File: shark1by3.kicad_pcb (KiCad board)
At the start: 2 copper layers, 57.2 x 46 mm, 26 parts, among them SW1 SW_Push_Reset, U1 PRTR5V0U2X, U2 ATmega32U4-A, X1 16MHz

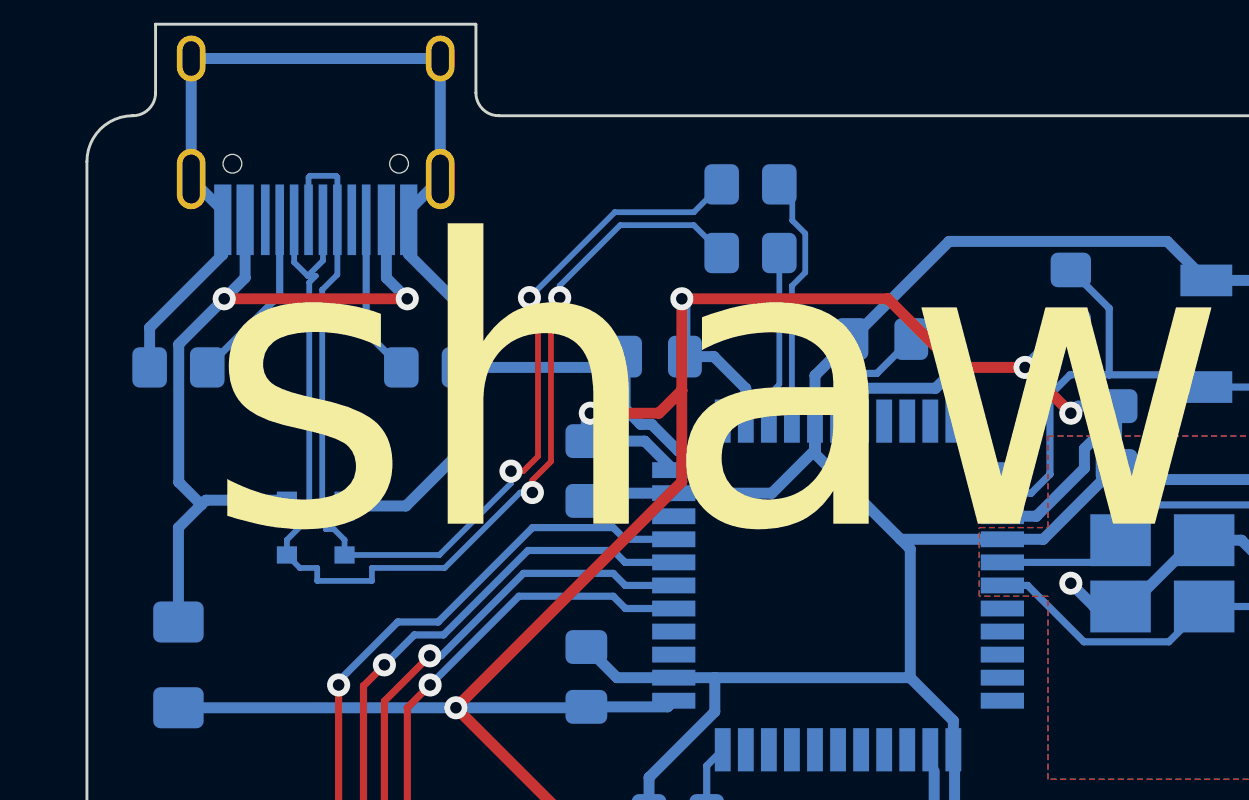
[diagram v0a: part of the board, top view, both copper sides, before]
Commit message: shorten data lines
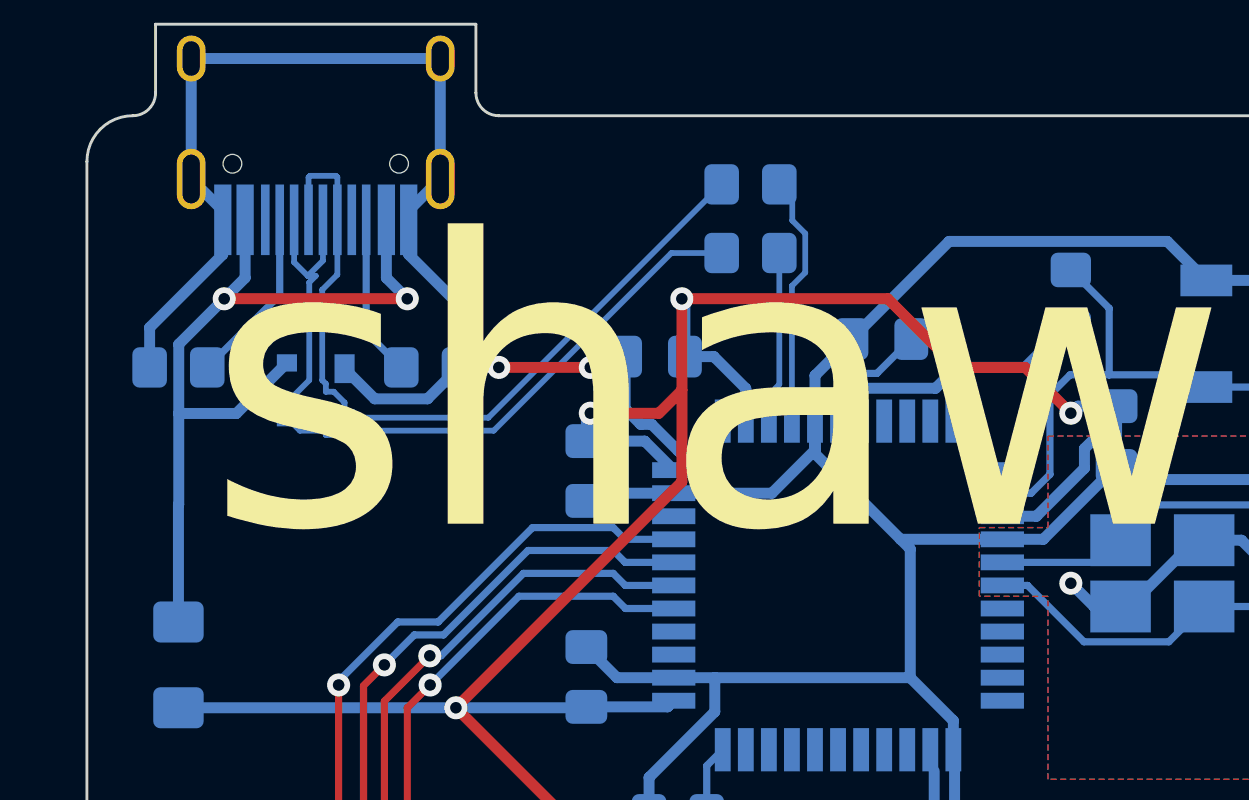
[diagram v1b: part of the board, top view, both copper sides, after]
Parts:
- moved U1 4.76 mm to (134.9, 120.7)
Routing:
- net DN: track 39.8 -> 28.0 mm, vias 2 -> 0
- net DP: track 38.6 -> 28.0 mm, vias 2 -> 0
- net GND: track 157.0 -> 154.2 mm, vias 3 -> 5
- net +5V: track 101.2 -> 103.6 mm, vias 7 -> 6
- net VCC: track 28.0 -> 28.8 mm

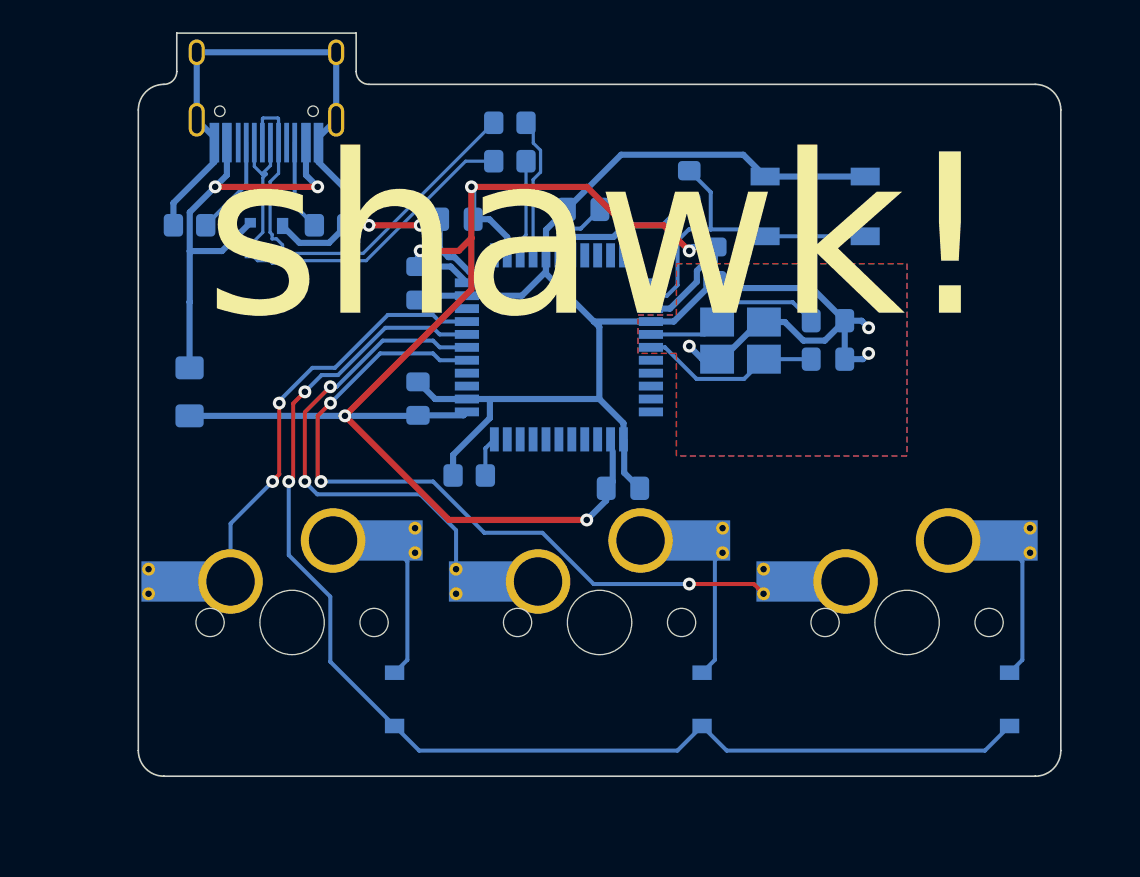
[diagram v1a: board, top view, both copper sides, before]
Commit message: add scuffed mounting holes
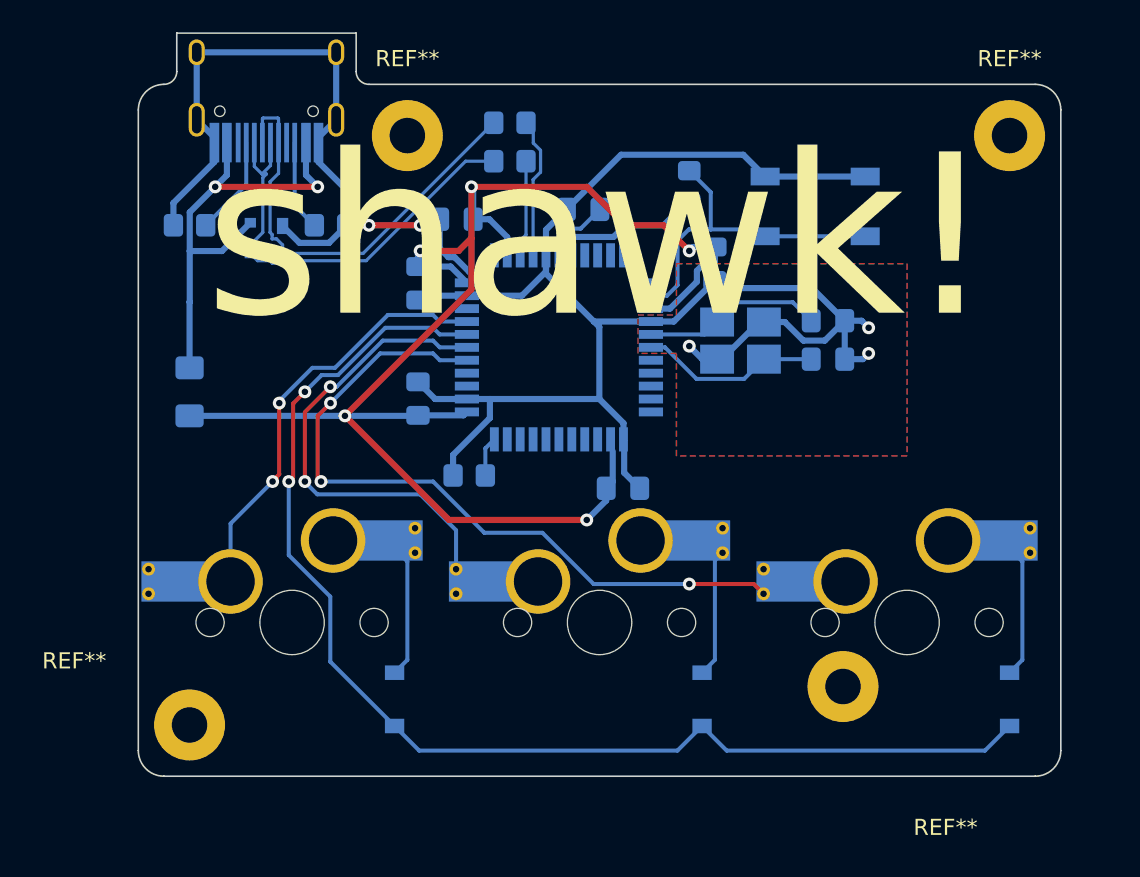
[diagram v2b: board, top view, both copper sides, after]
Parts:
- added REF**: MountingHole_2.2mm_M2_Pad, MountingHole:MountingHole_2.2mm_M2_Pad, F.Cu at (181.0, 114.3)
- added REF**: MountingHole_2.2mm_M2_Pad, MountingHole:MountingHole_2.2mm_M2_Pad, F.Cu at (170.7, 148.4)
- added REF**: MountingHole_2.2mm_M2_Pad, MountingHole:MountingHole_2.2mm_M2_Pad, F.Cu at (130.2, 150.8)
- added REF**: MountingHole_2.2mm_M2_Pad, MountingHole:MountingHole_2.2mm_M2_Pad, F.Cu at (143.7, 114.3)
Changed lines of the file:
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@@
   (net 44 "DN")
   (net 45 "DP")
+  (footprint "MountingHole:MountingHole_2.2mm_M2_Pad" (layer "F.Cu")
+    (at 180.975 114.3)
+    (descr "Mounting Hole 2.2mm, M2")
+    (tags "mounting hole 2.2mm m2")
+    (attr exclude_from_pos_files exclude_from_bom)
+    (fp_text reference "REF**" (at 0 -4.7625) (layer "F.SilkS")
+      (effects (font (size 1 1) (thickness 0.15)))
+    )
+    (fp_text value "MountingHole_2.2mm_M2_Pad" (at 0 3.2) (layer "F.Fab")
+      (effects (font (size 1 1) (thickness 0.15)))
+    )
+    (fp_text user "${REFERENCE}" (at 0 0) (layer "F.Fab")
+      (effects (font (size 1 1) (thickness 0.15)))
+    )
+    (fp_circle (center 0 0) (end 2.2 0) (layer "Cmts.User") (width 0.15) (fill none))
+    (fp_circle (center 0 0) (end 2.45 0) (layer "F.CrtYd") (width 0.05) (fill none))
+    (pad "1" thru_hole circle (at 0 0) (size 4.4 4.4) (drill 2.2) (layers *.Cu *.Mask))
+  )
   (footprint "MX_Only:MXOnly-1U-Hotswap-Antishear" (layer "F.Cu")
     (at 174.625 144.4625)
@@
     )
   )
+  (footprint "MountingHole:MountingHole_2.2mm_M2_Pad" (layer "F.Cu")
+    (at 170.65625 148.43125)
+    (descr "Mounting Hole 2.2mm, M2")
+    (tags "mounting hole 2.2mm m2")
+    (attr exclude_from_pos_files exclude_from_bom)
+    (fp_text reference "REF**" (at 6.35 8.73125) (layer "F.SilkS")
+      (effects (font (size 1 1) (thickness 0.15)))
+    )
+    (fp_text value "MountingHole_2.2mm_M2_Pad" (at 0 3.2) (layer "F.Fab")
+      (effects (font (size 1 1) (thickness 0.15)))
+    )
+    (fp_text user "${REFERENCE}" (at 0 0) (layer "F.Fab")
+      (effects (font (size 1 1) (thickness 0.15)))
+    )
+    (fp_circle (center 0 0) (end 2.2 0) (layer "Cmts.User") (width 0.15) (fill none))
+    (fp_circle (center 0 0) (end 2.45 0) (layer "F.CrtYd") (width 0.05) (fill none))
+    (pad "1" thru_hole circle (at 0 0) (size 4.4 4.4) (drill 2.2) (layers *.Cu *.Mask))
+  )
   (footprint "MX_Only:MXOnly-1U-Hotswap-Antishear" (layer "F.Cu")
     (at 155.575 144.4625)
@@
     )
   )
+  (footprint "MountingHole:MountingHole_2.2mm_M2_Pad" (layer "F.Cu")
+    (at 130.175 150.8125)
+    (descr "Mounting Hole 2.2mm, M2")
+    (tags "mounting hole 2.2mm m2")
+    (attr exclude_from_pos_files exclude_from_bom)
+    (fp_text reference "REF**" (at -7.14375 -3.96875) (layer "F.SilkS")
+      (effects (font (size 1 1) (thickness 0.15)))
+    )
+    (fp_text value "MountingHole_2.2mm_M2_Pad" (at 0 3.2) (layer "F.Fab")
+      (effects (font (size 1 1) (thickness 0.15)))
+    )
+    (fp_text user "${REFERENCE}" (at 0 0) (layer "F.Fab")
+      (effects (font (size 1 1) (thickness 0.15)))
+    )
+    (fp_circle (center 0 0) (end 2.2 0) (layer "Cmts.User") (width 0.15) (fill none))
+    (fp_circle (center 0 0) (end 2.45 0) (layer "F.CrtYd") (width 0.05) (fill none))
+    (pad "1" thru_hole circle (at 0 0) (size 4.4 4.4) (drill 2.2) (layers *.Cu *.Mask))
+  )
+  (footprint "MountingHole:MountingHole_2.2mm_M2_Pad" (layer "F.Cu")
+    (at 143.66875 114.3)
+    (descr "Mounting Hole 2.2mm, M2")
+    (tags "mounting hole 2.2mm m2")
+    (attr exclude_from_pos_files exclude_from_bom)
+    (fp_text reference "REF**" (at 0 -4.7625) (layer "F.SilkS")
+      (effects (font (size 1 1) (thickness 0.15)))
+    )
+    (fp_text value "MountingHole_2.2mm_M2_Pad" (at 0 3.2) (layer "F.Fab")
+      (effects (font (size 1 1) (thickness 0.15)))
+    )
+    (fp_text user "${REFERENCE}" (at 0 0) (layer "F.Fab")
+      (effects (font (size 1 1) (thickness 0.15)))
+    )
+    (fp_circle (center 0 0) (end 2.2 0) (layer "Cmts.User") (width 0.15) (fill none))
+    (fp_circle (center 0 0) (end 2.45 0) (layer "F.CrtYd") (width 0.05) (fill none))
+    (pad "1" thru_hole circle (at 0 0) (size 4.4 4.4) (drill 2.2) (layers *.Cu *.Mask))
+  )
   (footprint "Resistor_SMD:R_0805_2012Metric_Pad1.20x1.40mm_HandSolder" (layer "B.Cu")
